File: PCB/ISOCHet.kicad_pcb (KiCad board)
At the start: 2 copper layers, 57.1 x 38.1 mm, 19 parts, among them J1 USB_C_Receptacle_USB2.0, J2 Conn_01x08_Pin, SW0 BOOT, SW1 TAB, SW2 ENTER, SW3 CAPS, SW4 CAPS_STEP1.5, SW5 CAPS_STEP1.25, U1 CH552G, U2 USBLC6-2P6

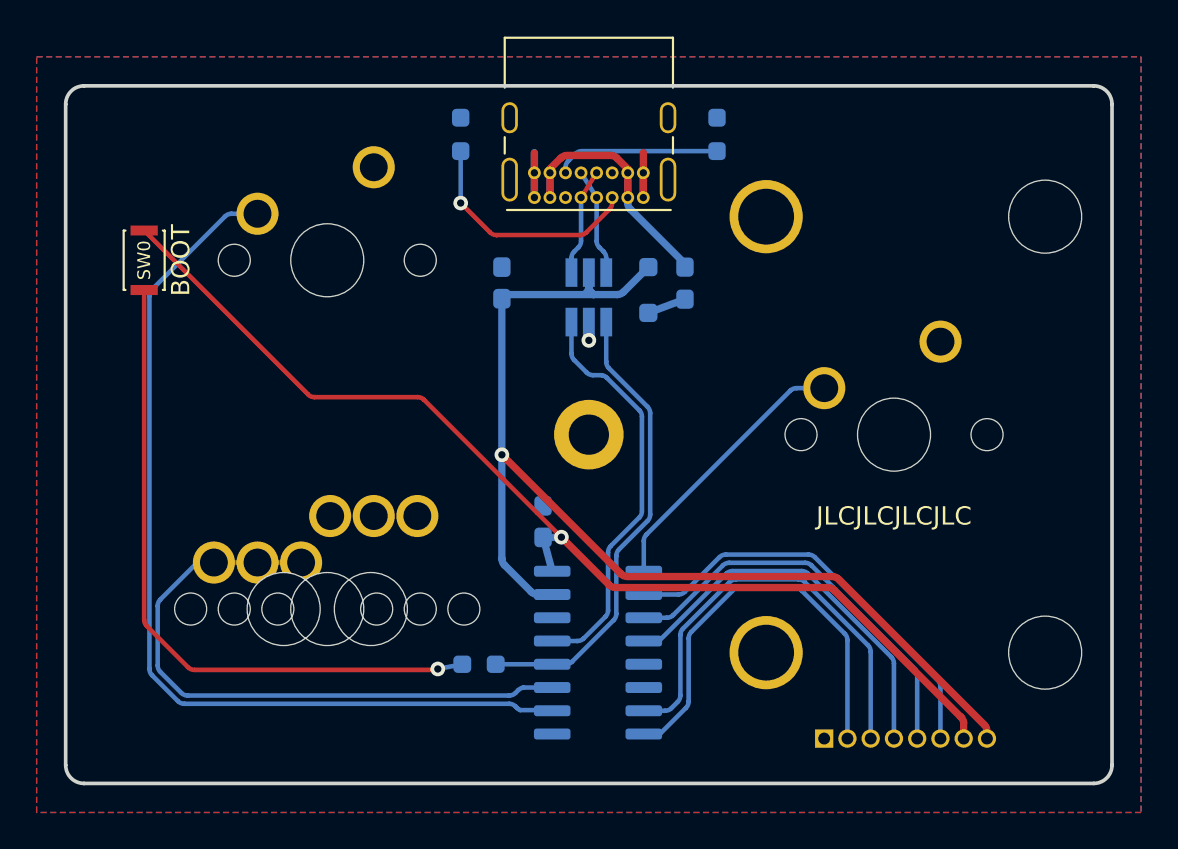
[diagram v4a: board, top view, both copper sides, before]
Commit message: Rotate ISO stabiliser, improve STEP export
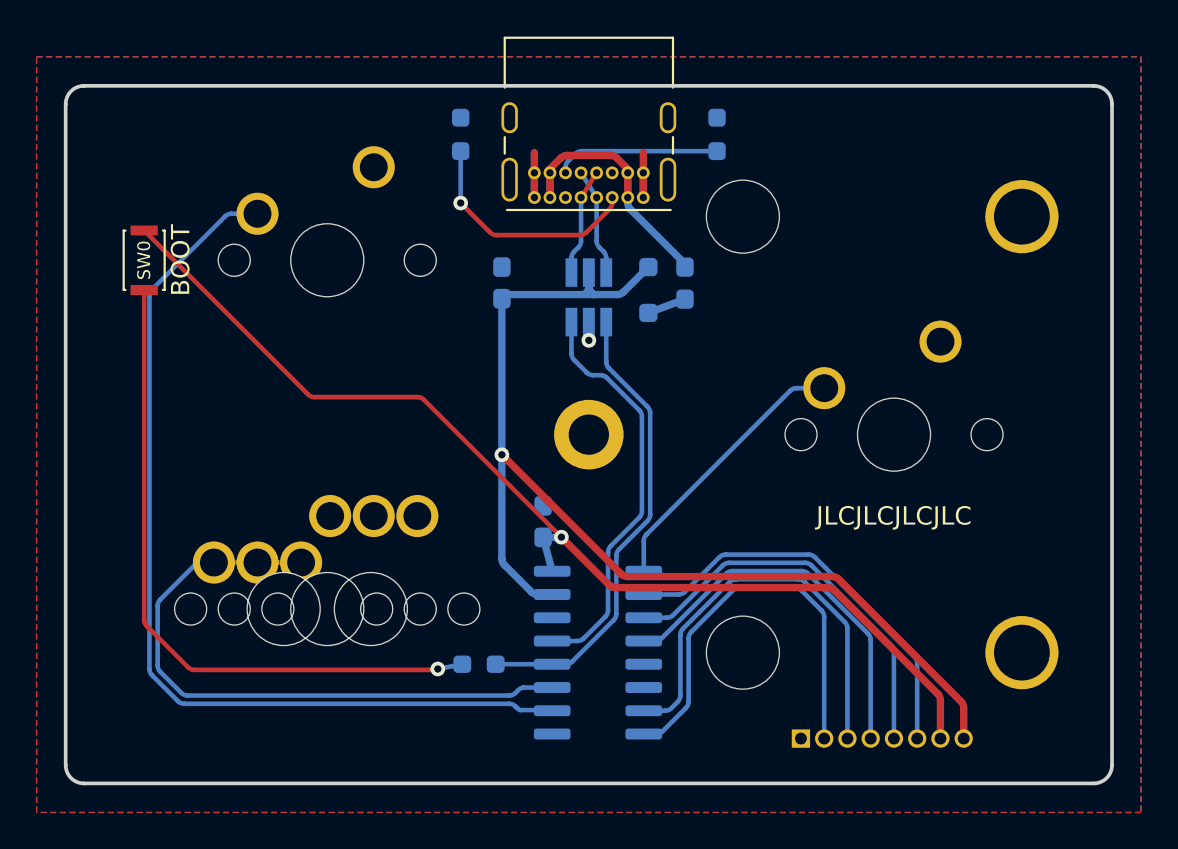
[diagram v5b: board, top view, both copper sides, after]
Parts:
- H2: footprint PCM_marbastlib-mx:STAB_MX_P_ISO -> PCM_marbastlib-mx:STAB_MX_P_ISO-ROT
- moved J2 1.27 mm to (170.3, 73.8)
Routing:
- net Net-(J2-Pin_2): track 23.3 -> 22.7 mm
- net Net-(J2-Pin_5): track 22.2 -> 21.7 mm
- net Net-(J2-Pin_6): track 23.0 -> 22.4 mm
- net VCC: track 61.0 -> 60.5 mm
- net Net-(J2-Pin_3): track 23.9 -> 23.4 mm
- net Net-(J2-Pin_4): track 20.7 -> 20.1 mm
- net +3V3: track 59.7 -> 59.1 mm

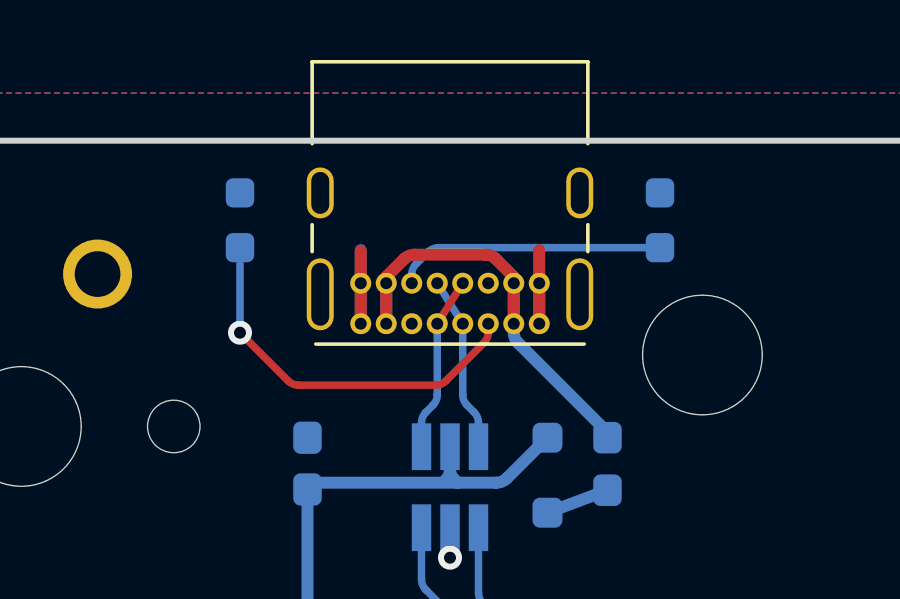
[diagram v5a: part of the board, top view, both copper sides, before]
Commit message: Move CC resistors away from PCB edge
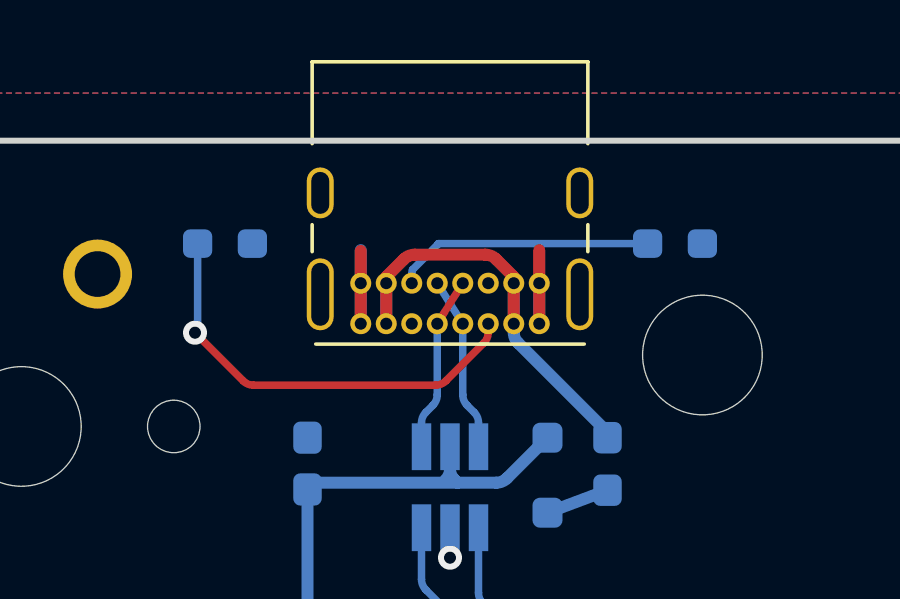
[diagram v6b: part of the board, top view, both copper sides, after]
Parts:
- moved R1 0.92 mm to (151.2, 41.5), turned to 0 degrees
- moved R2 0.92 mm to (166.2, 41.5), turned to 0 degrees
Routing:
- net Net-(J1-CC1): track 12.9 -> 14.6 mm
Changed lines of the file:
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@@
   )
   (footprint "Resistor_SMD:R_0603_1608Metric_Pad0.98x0.95mm_HandSolder" (layer "B.Cu")
-    (at 165.75 40.7525 90)
+    (at 166.25 41.53)
     (descr "Resistor SMD 0603 (1608 Metric), square (rectangular) end terminal, IPC_7351 nominal with elongated pad for handsoldering. (Body size source: IPC-SM-782 page 72, https://www.pcb-3d.com/wordpress/wp-content/uploads/ipc-sm-782a_amendment_1_and_2.pdf), generated with kicad-footprint-generator")
     (tags "resistor handsolder")
@@
     (property "ki_keywords" "R res resistor")
     (attr smd)
-    (fp_text reference "R2" (at 0 1.43 90) (layer "B.SilkS")
+    (fp_text reference "R2" (at 0 -1.36) (layer "B.SilkS")
         (effects (font (size 1 1) (thickness 0.15)) (justify mirror))
     )
-    (fp_text value "5.1k" (at 0 -1.43 90) (layer "B.Fab")
+    (fp_text value "5.1k" (at 0 -1.43) (layer "B.Fab")
         (effects (font (size 1 1) (thickness 0.15)) (justify mirror))
     )
-    (fp_text user "${REFERENCE}" (at 0 0 90) (layer "B.Fab")
+    (fp_text user "${REFERENCE}" (at 0 0) (layer "B.Fab")
         (effects (font (size 0.4 0.4) (thickness 0.06)) (justify mirror))
     )
@@
     (fp_line (start 0.8 0.4125) (end 0.8 -0.4125)
       (stroke (width 0.1) (type solid)) (layer "B.Fab"))
-    (pad "1" smd roundrect (at -0.9125 0 90) (size 0.975 0.95) (layers "B.Cu" "B.Paste" "B.Mask") (roundrect_rratio 0.25)
+    (pad "1" smd roundrect (at -0.9125 0) (size 0.975 0.95) (layers "B.Cu" "B.Paste" "B.Mask") (roundrect_rratio 0.25)
       (net 9 "Net-(J1-CC2)") (pintype "passive"))
-    (pad "2" smd roundrect (at 0.9125 0 90) (size 0.975 0.95) (layers "B.Cu" "B.Paste" "B.Mask") (roundrect_rratio 0.25)
+    (pad "2" smd roundrect (at 0.9125 0) (size 0.975 0.95) (layers "B.Cu" "B.Paste" "B.Mask") (roundrect_rratio 0.25)
       (net 2 "GND") (pintype "passive"))
     (model "${KICAD6_3DMODEL_DIR}/Resistor_SMD.3dshapes/R_0603_1608Metric.wrl"
@@
   )
   (footprint "Resistor_SMD:R_0603_1608Metric_Pad0.98x0.95mm_HandSolder" (layer "B.Cu")
-    (at 151.75 40.7525 90)
+    (at 151.25 41.53)
     (descr "Resistor SMD 0603 (1608 Metric), square (rectangular) end terminal, IPC_7351 nominal with elongated pad for handsoldering. (Body size source: IPC-SM-782 page 72, https://www.pcb-3d.com/wordpress/wp-content/uploads/ipc-sm-782a_amendment_1_and_2.pdf), generated with kicad-footprint-generator")
     (tags "resistor handsolder")
@@
     (property "ki_keywords" "R res resistor")
     (attr smd)
-    (fp_text reference "R1" (at 0 -1.36 90) (layer "B.SilkS")
+    (fp_text reference "R1" (at 0 -1.36) (layer "B.SilkS")
         (effects (font (size 1 1) (thickness 0.15)) (justify mirror))
     )
-    (fp_text value "5.1k" (at 0 -1.43 90) (layer "B.Fab")
+    (fp_text value "5.1k" (at 0 -1.43) (layer "B.Fab")
         (effects (font (size 1 1) (thickness 0.15)) (justify mirror))
     )
-    (fp_text user "${REFERENCE}" (at 0 0 90) (layer "B.Fab")
+    (fp_text user "${REFERENCE}" (at 0 0) (layer "B.Fab")
         (effects (font (size 0.4 0.4) (thickness 0.06)) (justify mirror))
     )
@@
     (fp_line (start 0.8 0.4125) (end 0.8 -0.4125)
       (stroke (width 0.1) (type solid)) (layer "B.Fab"))
-    (pad "1" smd roundrect (at -0.9125 0 90) (size 0.975 0.95) (layers "B.Cu" "B.Paste" "B.Mask") (roundrect_rratio 0.25)
+    (pad "1" smd roundrect (at -0.9125 0) (size 0.975 0.95) (layers "B.Cu" "B.Paste" "B.Mask") (roundrect_rratio 0.25)
       (net 5 "Net-(J1-CC1)") (pintype "passive"))
-    (pad "2" smd roundrect (at 0.9125 0 90) (size 0.975 0.95) (layers "B.Cu" "B.Paste" "B.Mask") (roundrect_rratio 0.25)
+    (pad "2" smd roundrect (at 0.9125 0) (size 0.975 0.95) (layers "B.Cu" "B.Paste" "B.Mask") (roundrect_rratio 0.25)
       (net 2 "GND") (pintype "passive"))
     (model "${KICAD6_3DMODEL_DIR}/Resistor_SMD.3dshapes/R_0603_1608Metric.wrl"
@@
   (segment (start 160.875 44.2) (end 160.875 44.487867) (width 0.4) (layer "B.Cu") (net 4))
   (arc (start 161.021447 44.841421) (mid 160.91306 44.679209) (end 160.875 44.487867) (width 0.4) (layer "B.Cu") (net 4))
+  (segment (start 152.207107 46.25) (end 158.262867 46.25) (width 0.25) (layer "F.Cu") (net 5))
+  (segment (start 158.616421 46.103553) (end 159.878554 44.84142) (width 0.25) (layer "F.Cu") (net 5))
   (segment (start 160.025 44.487867) (end 160.025 44.2) (width 0.25) (layer "F.Cu") (net 5))
-  (segment (start 151.75 44.5) (end 153.353554 46.103554) (width 0.25) (layer "F.Cu") (net 5))
-  (segment (start 158.616421 46.103553) (end 159.878554 44.84142) (width 0.25) (layer "F.Cu") (net 5))
-  (segment (start 153.707107 46.25) (end 158.262867 46.25) (width 0.25) (layer "F.Cu") (net 5))
-  (via (at 151.75 44.5) (size 0.8) (drill 0.4) (layers "F.Cu" "B.Cu") (net 5))
-  (arc (start 158.262867 46.25) (mid 158.454209 46.21194) (end 158.616421 46.103553) (width 0.25) (layer "F.Cu") (net 5))
-  (arc (start 160.025 44.487867) (mid 159.98694 44.679208) (end 159.878554 44.84142) (width 0.25) (layer "F.Cu") (net 5))
-  (arc (start 153.353554 46.103554) (mid 153.515766 46.21194) (end 153.707107 46.25) (width 0.25) (layer "F.Cu") (net 5))
-  (segment (start 151.75 44.5) (end 151.75 41.665) (width 0.25) (layer "B.Cu") (net 5))
+  (segment (start 150.25 44.5) (end 151.853554 46.103554) (width 0.25) (layer "F.Cu") (net 5))
+  (via (at 150.25 44.5) (size 0.8) (drill 0.4) (layers "F.Cu" "B.Cu") (net 5))
+  (arc (start 159.878554 44.84142) (mid 159.98694 44.679208) (end 160.025 44.487867) (width 0.25) (layer "F.Cu") (net 5))
+  (arc (start 158.262867 46.25) (mid 158.454207 46.211929) (end 158.616421 46.103553) (width 0.25) (layer "F.Cu") (net 5))
+  (arc (start 151.853554 46.103554) (mid 152.015766 46.21194) (end 152.207107 46.25) (width 0.25) (layer "F.Cu") (net 5))
+  (segment (start 150.25 44.5) (end 150.3375 44.4125) (width 0.25) (layer "B.Cu") (net 5))
+  (segment (start 150.3375 44.4125) (end 150.3375 41.53) (width 0.25) (layer "B.Cu") (net 5))
   (segment (start 159.175 44.2) (end 159.175 46.567893) (width 0.25) (layer "B.Cu") (net 6))
   (segment (start 159.7 47.507107) (end 159.7 48.3) (width 0.25) (layer "B.Cu") (net 6))
@@
   (arc (start 157.8 47.507107) (mid 157.83806 47.315766) (end 157.946446 47.153554) (width 0.25) (layer "B.Cu") (net 7))
   (arc (start 158.325 46.567893) (mid 158.28694 46.759235) (end 158.178553 46.921447) (width 0.25) (layer "B.Cu") (net 7))
-  (segment (start 157.621447 42.208579) (end 158.01858 41.811446) (width 0.25) (layer "B.Cu") (net 9))
-  (segment (start 158.372133 41.665) (end 165.75 41.665) (width 0.25) (layer "B.Cu") (net 9))
+  (segment (start 157.499889 42.400598) (end 158.360026 41.540461) (width 0.25) (layer "B.Cu") (net 9))
+  (segment (start 158.360026 41.540461) (end 158.360026 41.53) (width 0.25) (layer "B.Cu") (net 9))
   (segment (start 157.475 42.85) (end 157.475 42.562133) (width 0.25) (layer "B.Cu") (net 9))
-  (arc (start 158.372133 41.665) (mid 158.180792 41.70306) (end 158.01858 41.811446) (width 0.25) (layer "B.Cu") (net 9))
-  (arc (start 157.621447 42.208579) (mid 157.51306 42.370791) (end 157.475 42.562133) (width 0.25) (layer "B.Cu") (net 9))
+  (segment (start 158.360026 41.53) (end 165.3375 41.53) (width 0.25) (layer "B.Cu") (net 9))
+  (arc (start 157.475 42.562133) (mid 157.48206 42.480616) (end 157.499889 42.400598) (width 0.25) (layer "B.Cu") (net 9))
   (segment (start 159.7 51) (end 159.7 53.167157) (width 0.25) (layer "B.Cu") (net 11))
   (segment (start 160.25 63.772793) (end 160.25 66.929289) (width 0.25) (layer "B.Cu") (net 11))

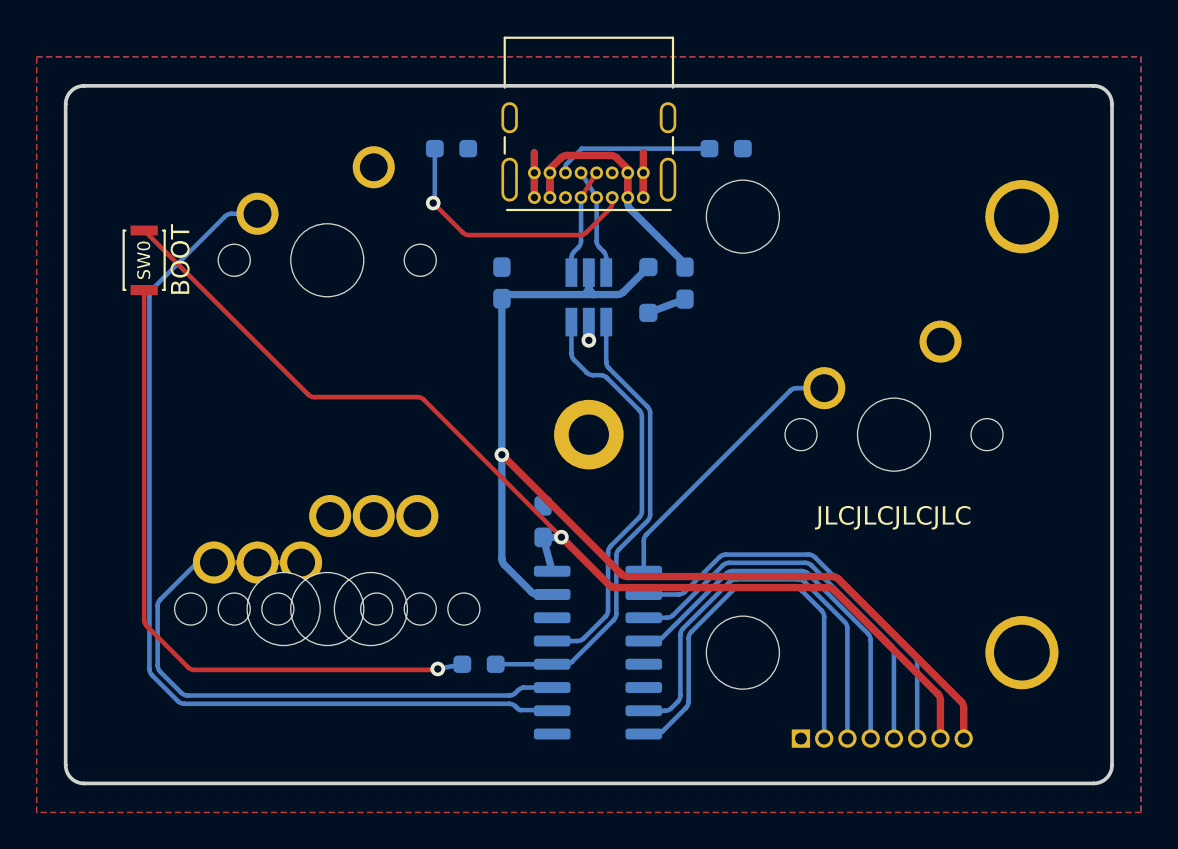
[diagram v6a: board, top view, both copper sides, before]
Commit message: Move components
 * Move decoupling capacitor C1 close to U1
 * Move U1 away from PCB edge
 * Align U1 with PCB centreline
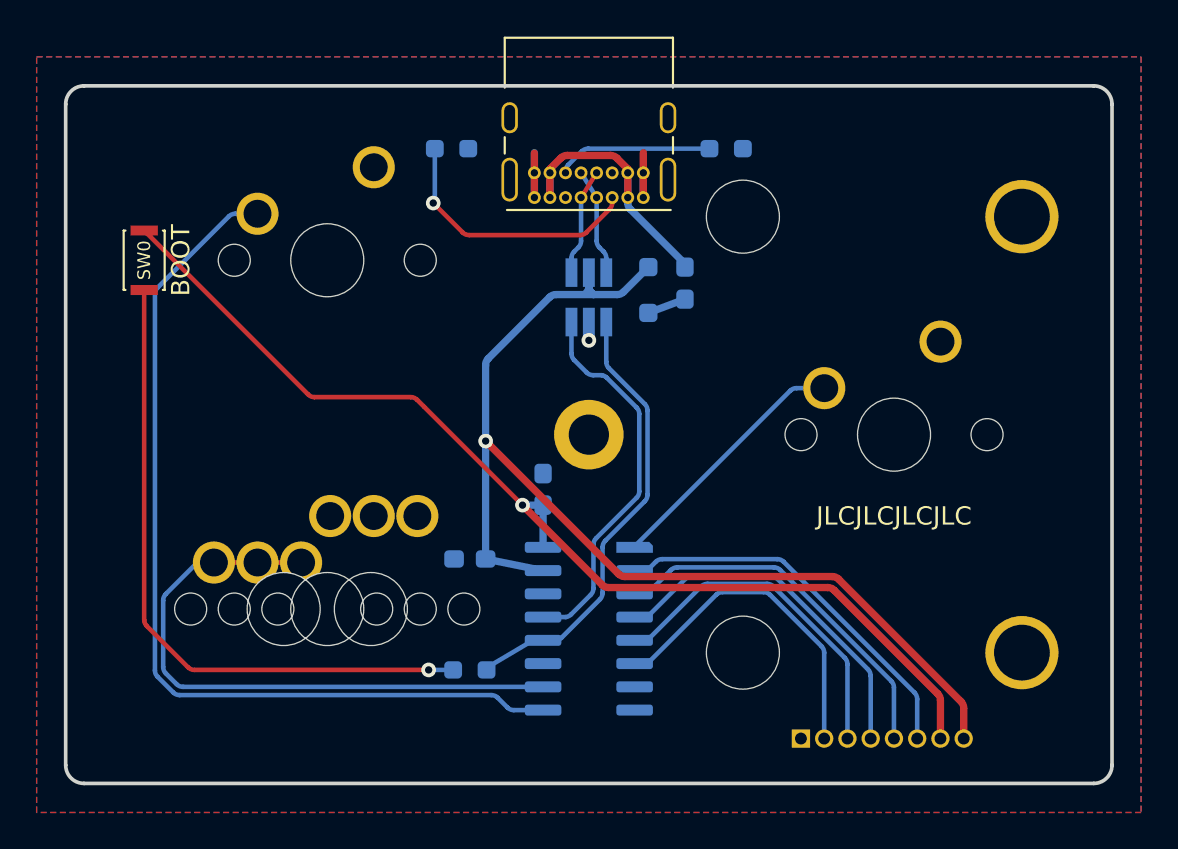
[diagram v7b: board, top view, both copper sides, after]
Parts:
- moved C1 15.2 mm to (152.2, 63.9), turned to 180 degrees
- moved C2 1.76 mm to (156.2, 60.1)
- moved U1 1.40 mm to (158.8, 67.8)
- moved R3 0.59 mm to (152.2, 70.0)
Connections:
- U1 pad 10: Tab -> Caps
- U1 pad 11: Caps -> unconnected-(U1-P3.4-Pad11)
- U1 pad 5: unconnected-(U1-P1.7-Pad5) -> Net-(J2-Pin_3)
- U1 pad 6: unconnected-(U1-RST-Pad6) -> Net-(J2-Pin_2)
- U1 pad 7: Net-(J2-Pin_3) -> unconnected-(U1-P3.1-Pad7)
- U1 pad 8: Net-(J2-Pin_2) -> unconnected-(U1-P3.0-Pad8)
- U1 pad 9: unconnected-(U1-P1.1-Pad9) -> Tab
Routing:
- net Net-(J2-Pin_2): track 22.7 -> 18.1 mm
- net Net-(J2-Pin_3): track 23.4 -> 18.8 mm
- net Net-(J2-Pin_5): track 21.7 -> 20.3 mm
- net Net-(J2-Pin_6): track 22.4 -> 21.0 mm
- net UDM: track 22.3 -> 20.9 mm
- net Caps: track 33.7 -> 32.5 mm
- net Enter: track 15.0 -> 14.0 mm
- net Tab: track 51.1 -> 50.2 mm
- net VCC: track 60.5 -> 61.2 mm
- net Net-(R3-Pad2): track 36.6 -> 36.0 mm
- net Net-(J2-Pin_4): track 20.1 -> 19.5 mm
- net UDP: track 24.6 -> 24.0 mm
- net +3V3: track 59.1 -> 59.6 mm
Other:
- board text removed: "•"
